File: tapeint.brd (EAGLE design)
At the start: 30 x 20 mm, 20 parts, among them U1 MCP6241

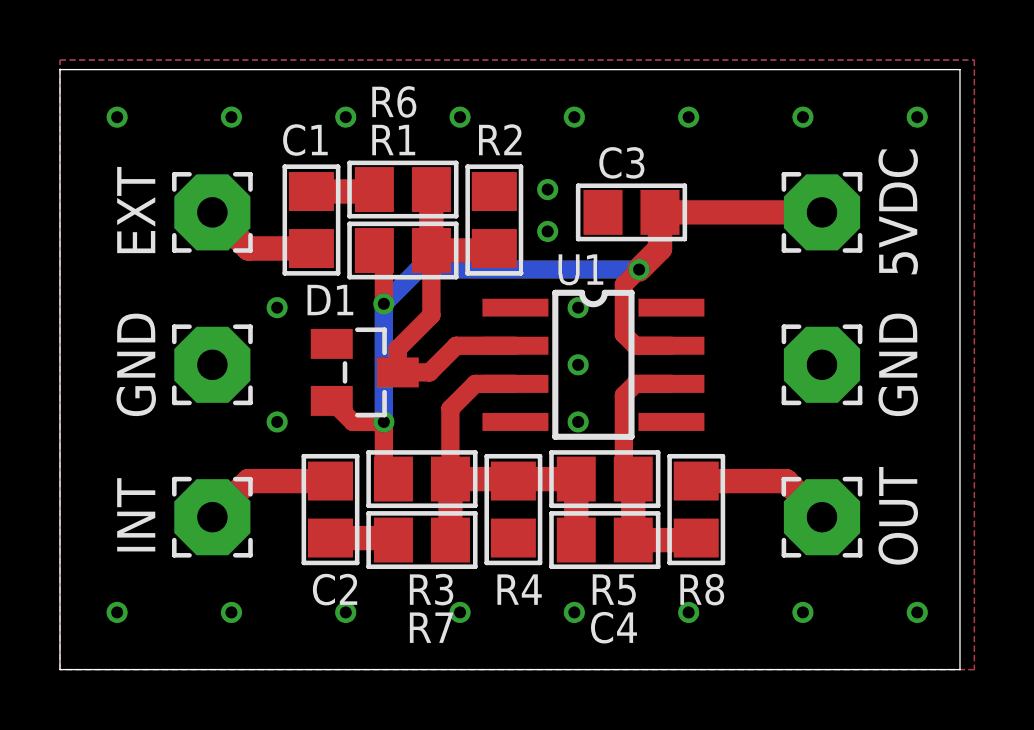
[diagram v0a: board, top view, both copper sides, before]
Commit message: Updated version with better 0805 footprints, gerbers in a zip file, and BOM/CPL data for jlcpcb
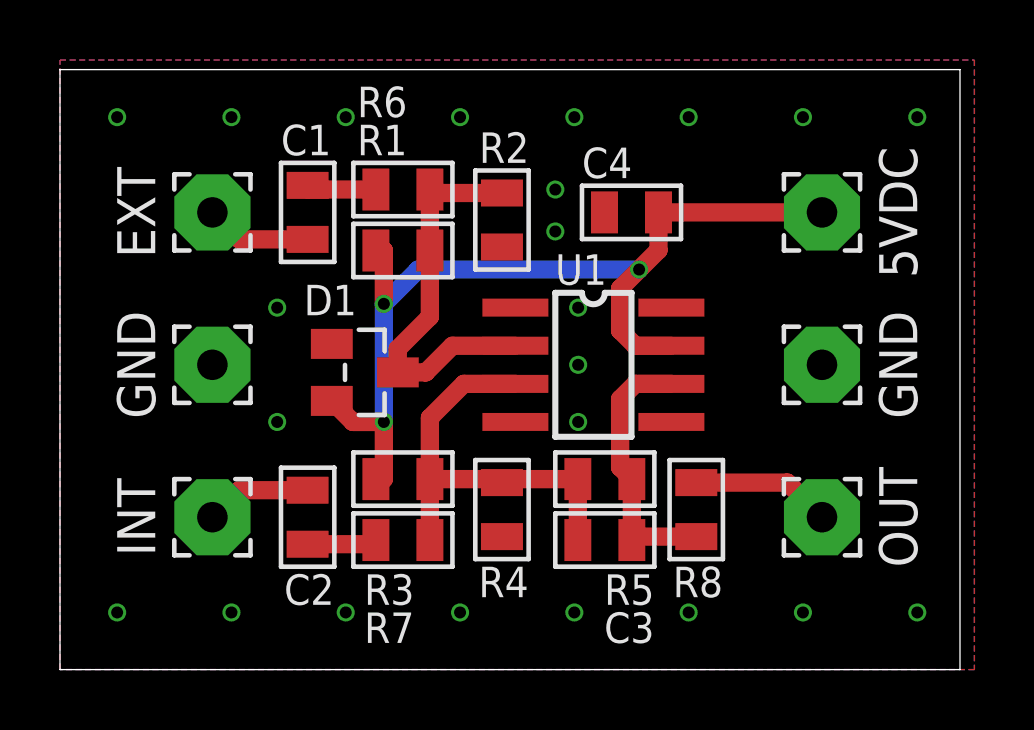
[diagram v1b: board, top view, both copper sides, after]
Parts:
- C1, C2: device rcl:C0805 -> jc-passive:0805
- C3: value 470n -> 47p; device rcl:C0805 -> jc-passive:0805
- C4: value 47p -> 1u; device rcl:C0805 -> jc-passive:0805
- R1, R2, R3, R4, R5, R6, R7, R8: device rcl:R0805 -> jc-passive:0805
- moved C3 11.0 mm to (18.2, 4.32), turned to 0 degrees
- moved C4 11.0 mm to (19.1, 15.2), turned to 180 degrees
- moved C2 0.80 mm to (8.26, 5.08)
- moved R3 0.63 mm to (11.4, 6.35)
- moved R7 0.63 mm to (11.4, 4.32)
- moved R4 0.38 mm to (14.7, 5.33)
- moved C1 0.28 mm to (8.26, 15.2)
- moved R2 0.25 mm to (14.7, 15.0), turned to 90 degrees
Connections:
- net +5V: now also C4.1; no longer C3.1
- net GND: now also C4.2; no longer C3.2
- net N$4: now also C3.1; no longer C4.1
- net OUT: now also C3.2; no longer C4.2
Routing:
- net N$4: track 13.2 -> 14.5 mm
- net N$8: track 4.44 -> 3.55 mm
